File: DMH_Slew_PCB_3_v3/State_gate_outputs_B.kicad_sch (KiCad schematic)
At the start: 25 parts, among them J10 TS_Jack_6.35mm_Sw, J9 TS_Jack_6.35mm_Sw, Q11 BC548, Q12 BC548, U3 TL074

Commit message: Adjustments after prototyping
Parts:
- R70: value 1k8 -> 2k2
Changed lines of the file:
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@@
 			)
 		)
-		(property "Value" "1k8"
+		(property "Value" "2k2"
 			(at 252.73 46.9899 0)
 			(effects

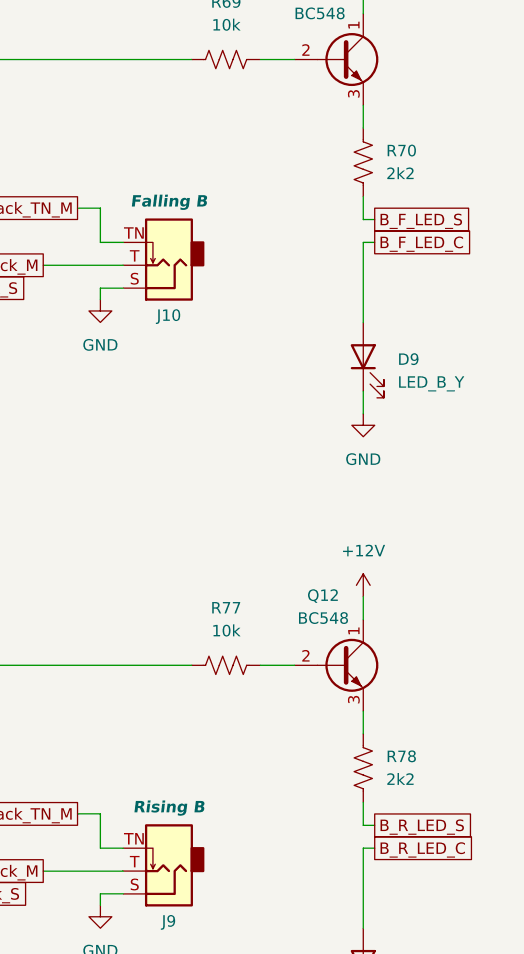
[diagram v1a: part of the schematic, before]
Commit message: Corrected PCB 2 switch positions
and Regenerated Gerbers
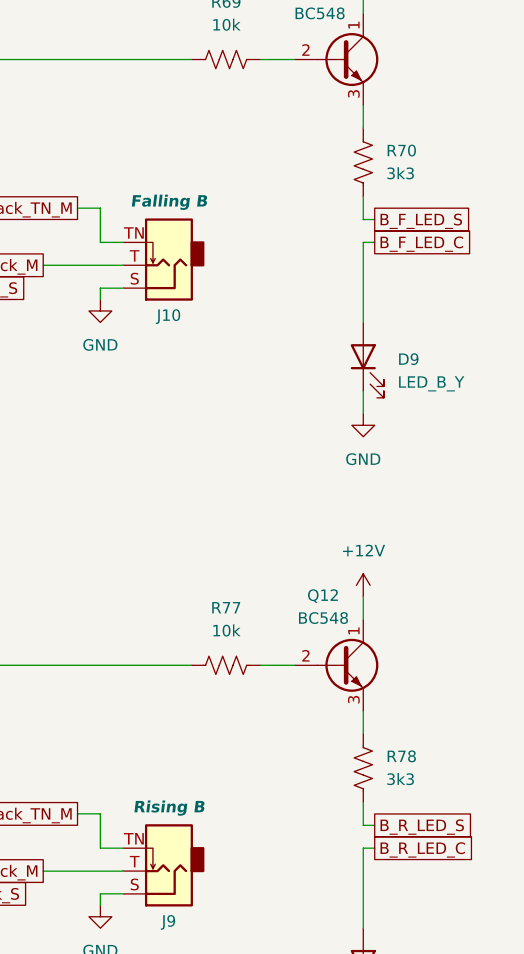
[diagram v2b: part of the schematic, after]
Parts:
- R70, R78: value 2k2 -> 3k3
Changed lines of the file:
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@@
 			)
 		)
-		(property "Value" "2k2"
+		(property "Value" "3k3"
 			(at 252.73 114.2999 0)
 			(effects
@@
 			)
 		)
-		(property "Value" "2k2"
+		(property "Value" "3k3"
 			(at 252.73 46.9899 0)
 			(effects

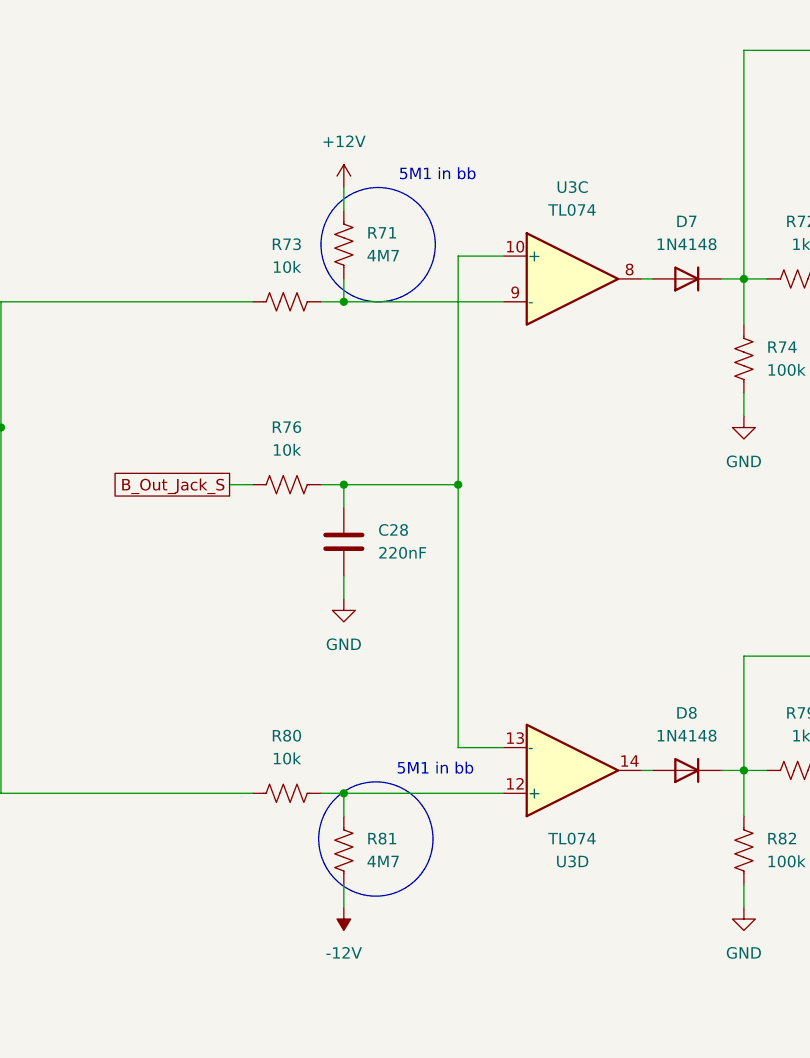
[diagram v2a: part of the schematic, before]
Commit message: Redesigned Main PCB
and regenerated Gerbers
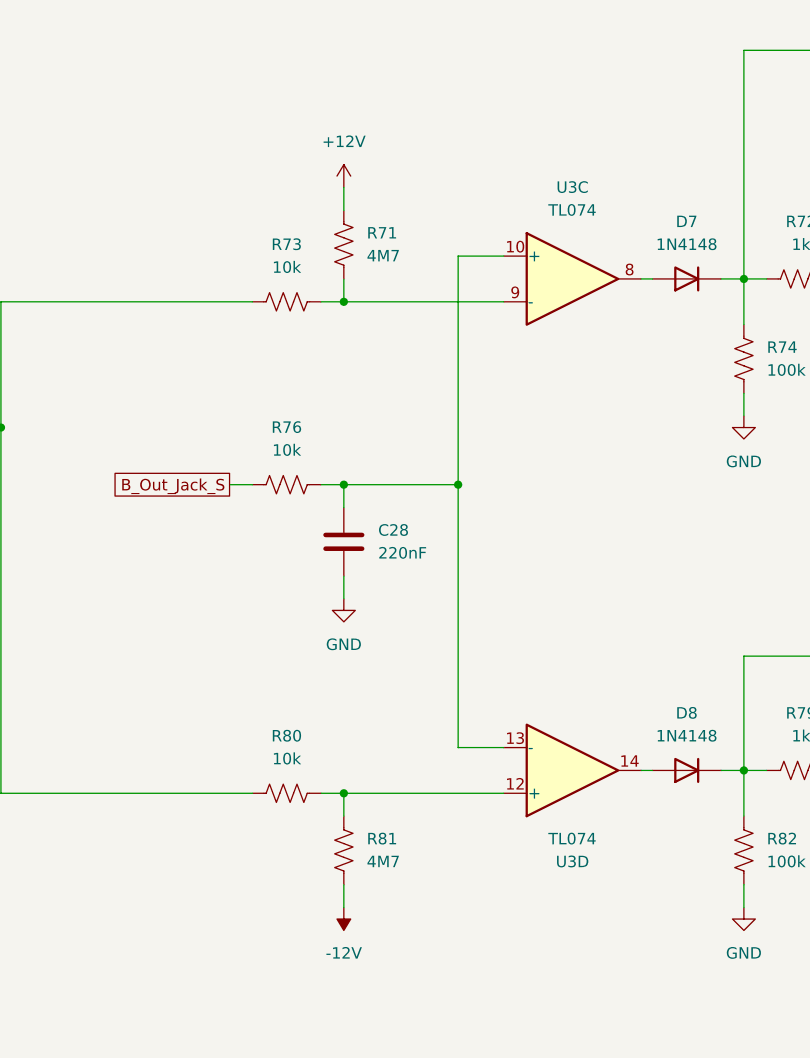
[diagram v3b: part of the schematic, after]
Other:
- note removed: "5M1 in bb"
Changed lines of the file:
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@@
 		(comment 1 "PCB for 5 cm Kosmo format synthesizer module")
-	)
-	(circle
-		(center 130.556 121.92)
-		(radius 6.35)
-		(stroke
-			(width 0)
-			(type default)
-		)
-		(fill
-			(type none)
-		)
-	)
-	(circle
-		(center 130.81 55.88)
-		(radius 6.35)
-		(stroke
-			(width 0)
-			(type default)
-		)
-		(fill
-			(type none)
-		)
-	)
-	(text "5M1 in bb"
-		(exclude_from_sim no)
-		(at 137.414 48.26 0)
-		(effects
-			(font
-				(size 1.27 1.27)
-			)
-		)
-	)
-	(text "5M1 in bb"
-		(exclude_from_sim no)
-		(at 137.16 114.3 0)
-		(effects
-			(font
-				(size 1.27 1.27)
-			)
-		)
 	)
 	(junction
